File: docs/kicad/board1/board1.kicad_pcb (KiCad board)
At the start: 2 copper layers, 61 x 90.2 mm, 33 parts, among them J1 12 IN, J2 5V Jump, J3 5V Test, J4 SENSOR_ASSY, J5 PUMP, J6 WS2812_B, J7 RS485, M1 BUCK01, M2 SD_TYP0, Q1 IRLZ44N, U1 RS485_MODULE, U2 ESP32_DEV_0

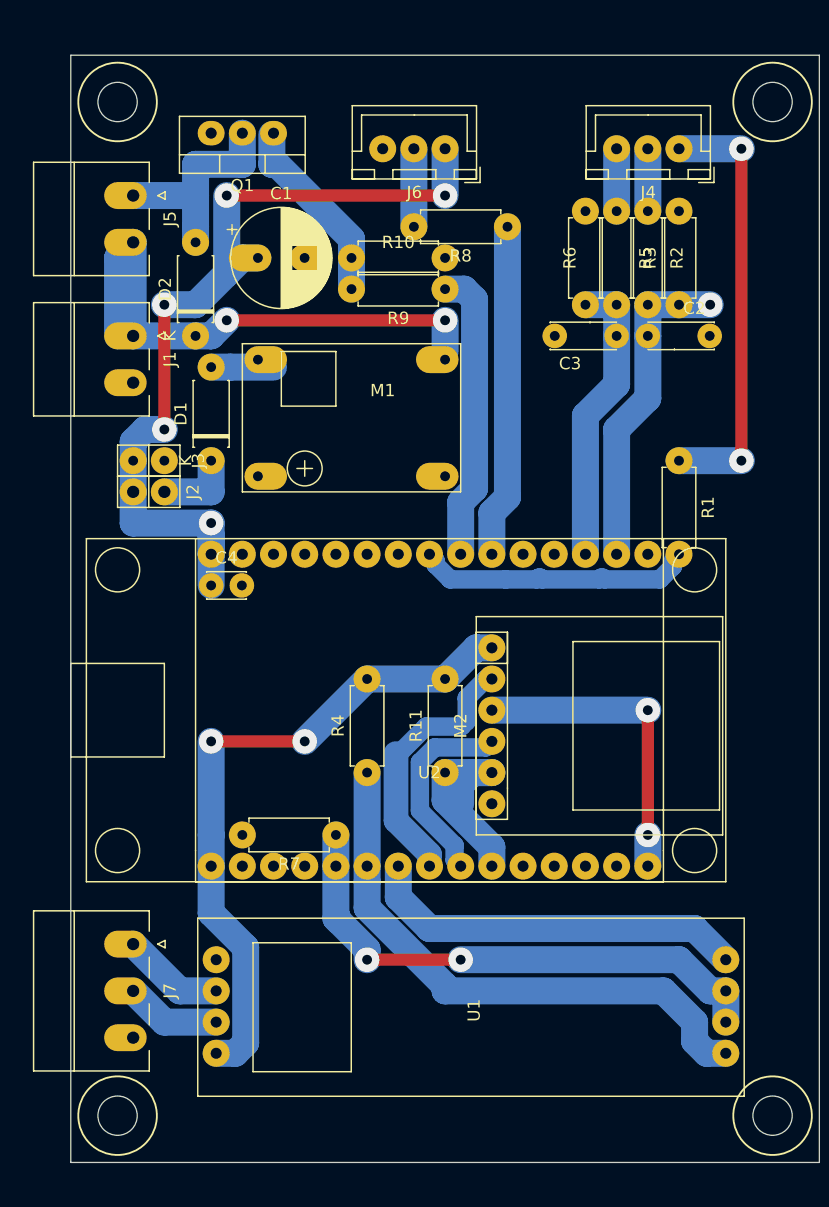
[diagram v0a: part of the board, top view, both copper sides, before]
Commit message: updated combined BOARD1 - single sensor, resistor silkscreen
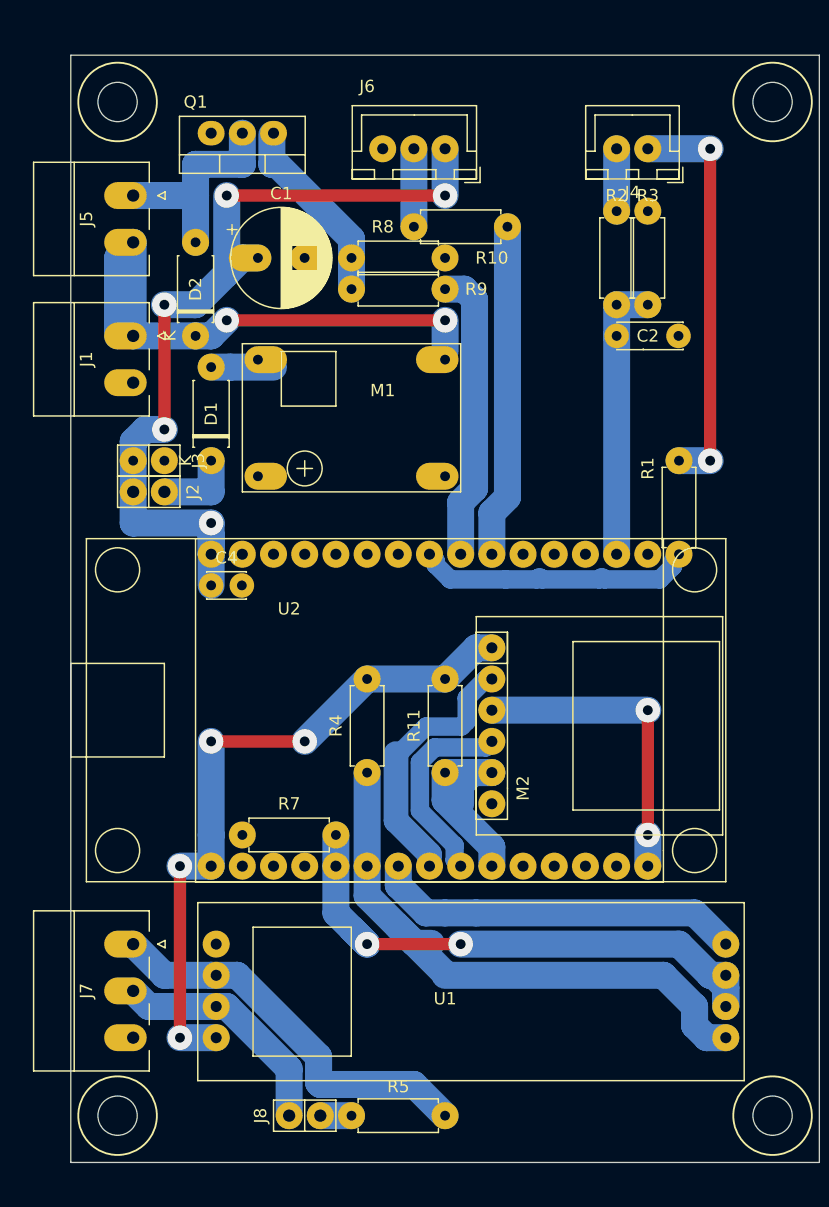
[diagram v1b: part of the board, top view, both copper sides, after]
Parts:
- removed C3: 2.2uf, 0_my_footprints:myCapTantulum2
- removed R6: 100K, 0_my_footprints:myResistor
- added J8: RS485_TERMINATOR, 0_my_footprints:myPinHeader_1x02, F.Cu at (58.4, 109.2)
- J4: value SENSOR_ASSY -> SENSOR; footprint 0_my_footprints:myJSTx03 -> 0_my_footprints:myJSTx02
- R5: value 1K -> 220
- moved R5 76.8 mm to (63.5, 109.2), turned to 0 degrees
- moved C2 2.54 mm to (87.6, 45.7)
- moved J4 2.54 mm to (87.6, 30.5)
- moved R3 2.54 mm to (87.6, 43.2)
- moved R2 2.54 mm to (85.1, 35.6)
- moved U1 1.27 mm to (94.0, 102.9)
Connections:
- net ROD_LOW renamed SENSOR_ROD
- net SENSOR_LOW renamed SENSOR
- R5 pad 1: ROD_HIGH -> Net-(J8-Pad2)
- R5 pad 2: SENSOR_HIGH -> RS485_B
- U2 pad 13: SENSOR_HIGH -> Net-(U2-Pad13)
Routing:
- net RS485_B: track 8.34 -> 32.4 mm
- net SENSOR_HIGH: track 23.9 -> 0.00 mm
- net RS485_A: track 7.81 -> 19.1 mm
- net ROD_HIGH: track 5.08 -> 0.00 mm
- net TX_EN: track 44.1 -> 47.8 mm
- net SENSOR: track 26.5 -> 22.9 mm, vias 1 -> 0
- net DRIVE_ROD: track 35.6 -> 33.0 mm
- net Net-(J8-Pad2): track 0.00 -> 2.54 mm
- net RX2: track 46.3 -> 48.2 mm
- net +3V3: track 54.5 -> 55.6 mm, vias 2 -> 4
- net TX2: track 31.3 -> 30.2 mm

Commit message: checkin board1 before milling
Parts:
- J4: footprint 0_my_footprints:myJSTx02 -> 0_my_footprints:myPheonix3x3.81_right
- J6: footprint 0_my_footprints:myJSTx03 -> 0_my_footprints:myPheonix3x3.81_right
- moved J4 5.35 mm to (86.4, 25.3)
- moved J6 5.35 mm to (72.4, 25.3)
- moved J5 1.27 mm to (45.7, 35.6)
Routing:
- net SENSOR_ROD: track 5.08 -> 11.2 mm
- net +5V: track 69.9 -> 75.1 mm, vias 5 -> 4
- net Net-(J6-Pad2): track 6.35 -> 11.4 mm
- net PUMP+: track 44.2 -> 41.2 mm
- net DRIVE_ROD: track 33.0 -> 35.9 mm
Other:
- board size 61 x 90.2 mm -> 61 x 92.7 mm

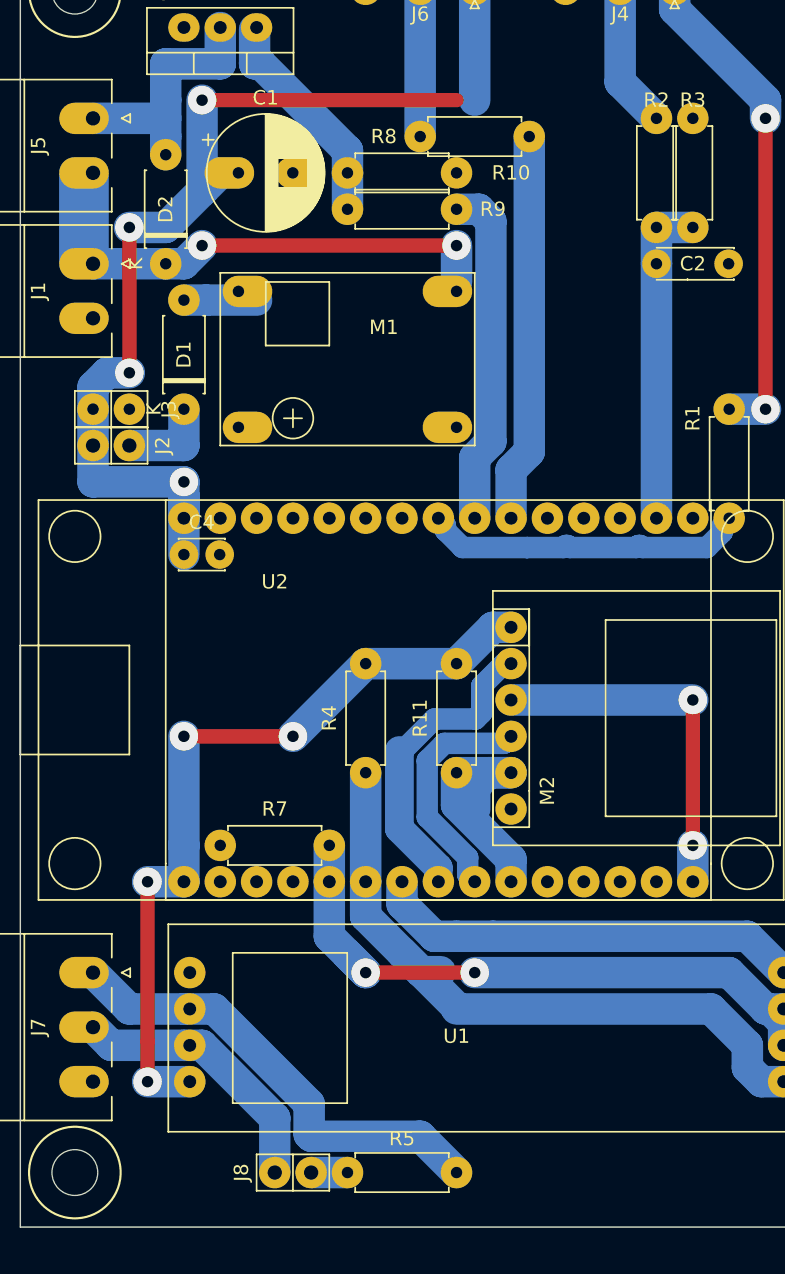
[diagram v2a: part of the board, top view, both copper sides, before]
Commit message: build airco PCB and print box
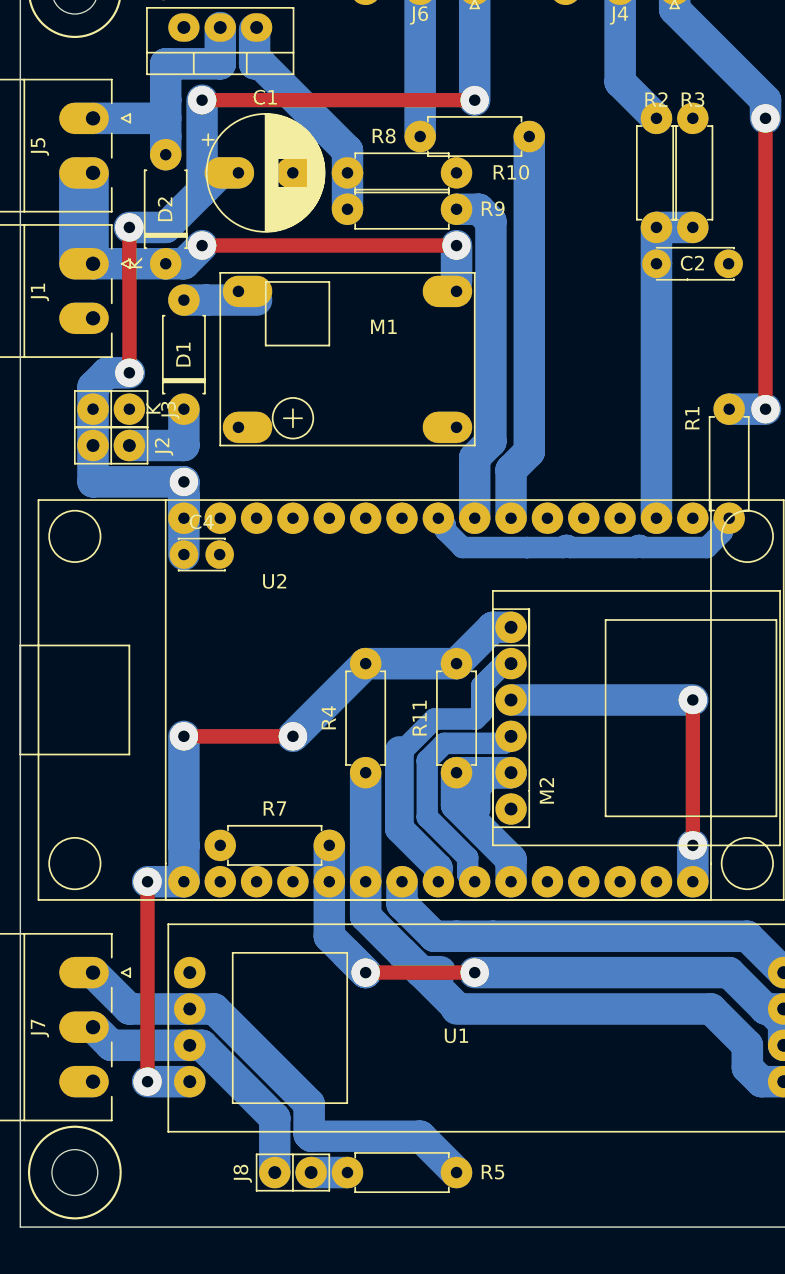
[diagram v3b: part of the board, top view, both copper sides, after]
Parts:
- R5: value 220 -> 120
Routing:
- net +5V: track 75.1 -> 76.3 mm, vias 4 -> 5
